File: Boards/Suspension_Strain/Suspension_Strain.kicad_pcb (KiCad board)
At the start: 2 copper layers, 57.2 x 57.2 mm, 146 parts, among them J1 CONN_02X03, J101 MM_F_RA_20, J102 MM_F_RA_08, U1 MCP2561-E_SN, U1001 MCP6001T-I-LT, U101 TPS560430YF, U102 74HC4051, U1101 MCP6001T-I-LT, U1201 MCP6001T-I-LT, U1301 MCP6001T-I-LT, U1401 MCP6001T-I-LT, U2 ATMEGA16M1, U301 MCP6001T-I-LT, U401 MCP6001T-I-LT, U501 MCP6001T-I-LT, U601 MCP6001T-I-LT, U701 MCP6001T-I-LT, U801 MCP6001T-I-LT, U901 MCP6001T-I-LT, Y1 Crystal_SMD

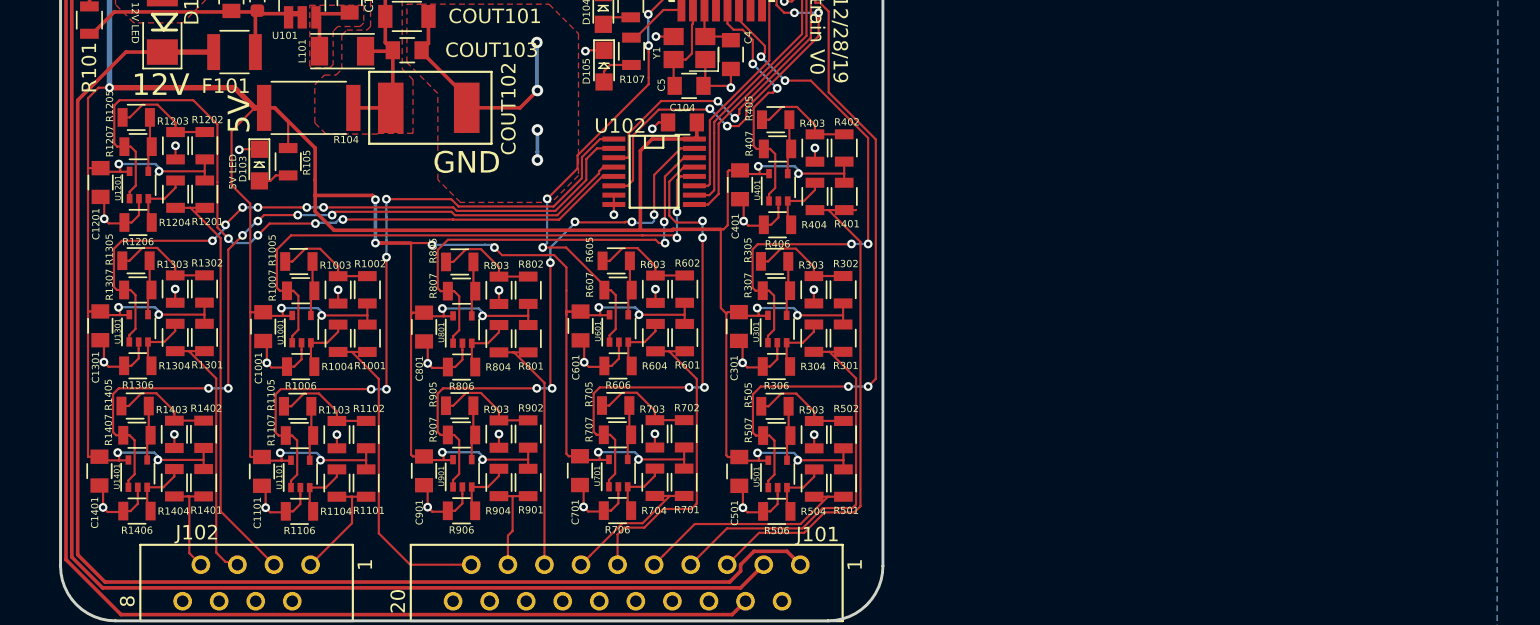
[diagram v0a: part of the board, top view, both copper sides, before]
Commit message: Remove excessive differential amplifiers
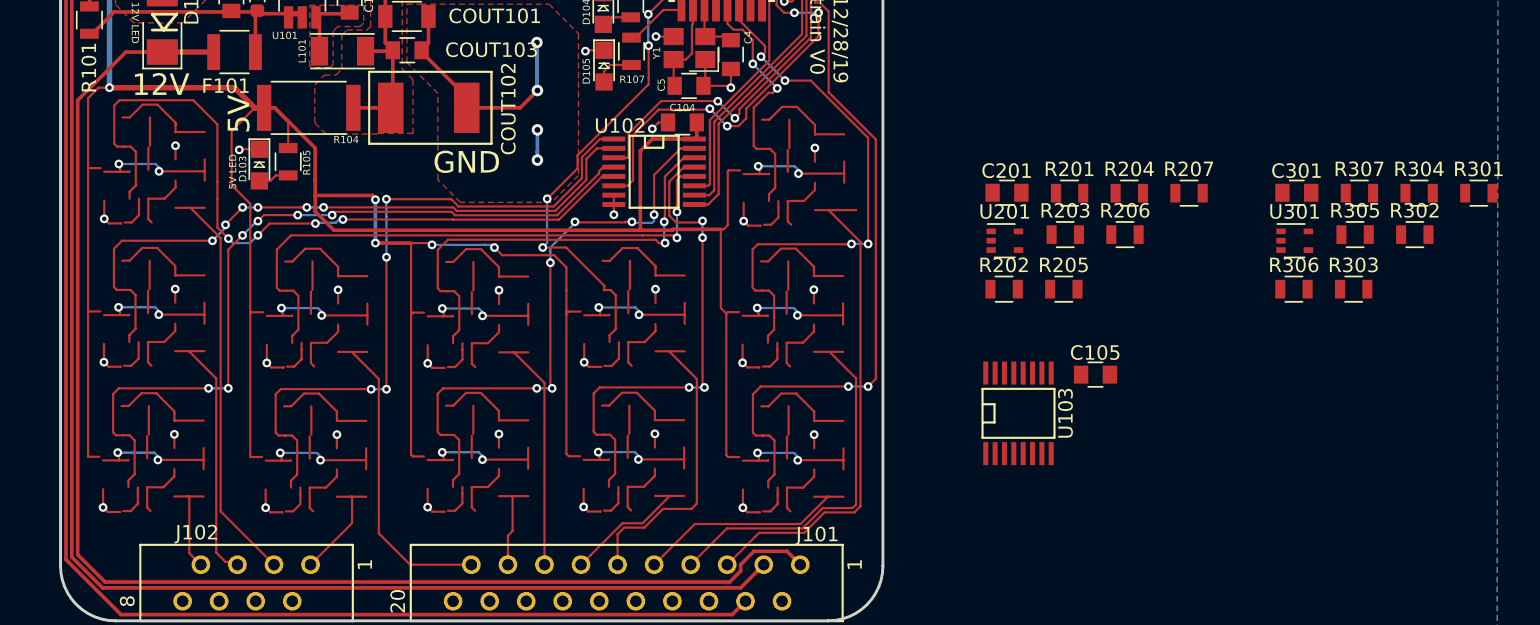
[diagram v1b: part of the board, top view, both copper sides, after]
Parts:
- removed C1001, C1101, C1201, C1301, C1401, C401, C501, C601, C701, C801, C901: C_0.1uF, footprints:C_0805_OEM
- removed G***: LOGO, footprints:Logo_Large
- removed R1001, R1002, R1003, R1004, R1005, R1101, R1102, R1103, R1104, R1105, R1201, R1202, R1203, R1204, R1205, R1301, R1302, R1303, R1304, R1305, R1401, R1402, R1403, R1404, R1405, R401, R402, R403, R404, R405, R501, R502, R503, R504, R505, R601, R602, R603, R604, R605, R701, R702, R703, R704, R705, R801, R802, R803, R804, R805, R901, R902, R903, R904, R905: R_120, footprints:R_0805_OEM
- removed R1006, R1007, R1106, R1107, R1206, R1207, R1306, R1307, R1406, R1407, R406, R407, R506, R507, R606, R607, R706, R707, R806, R807, R906, R907: R_4.99K, footprints:R_0805_OEM
- removed U1001, U1101, U1201, U1301, U1401, U401, U501, U601, U701, U801, U901: MCP6001T-I-LT, Package_TO_SOT_SMD:SOT-353_SC-70-5
- added C105: C_0.1uF, footprints:C_0805_OEM, F.Cu at (180.3, 128.1)
- added C201: C_0.1uF, footprints:C_0805_OEM, F.Cu at (174.1, 115.5)
- added R201: R_120, footprints:R_0805_OEM, F.Cu at (178.5, 115.5)
- added R202: R_120, footprints:R_0805_OEM, F.Cu at (173.9, 122.2)
- added R203: R_120, footprints:R_0805_OEM, F.Cu at (178.2, 118.4)
- added R204: R_120, footprints:R_0805_OEM, F.Cu at (182.6, 115.5)
- added R205: R_120, footprints:R_0805_OEM, F.Cu at (178.1, 122.2)
- added R206: R_4.99K, footprints:R_0805_OEM, F.Cu at (182.3, 118.4)
- added R207: R_4.99K, footprints:R_0805_OEM, F.Cu at (186.8, 115.5)
- added U103: 74HC4051, footprints:TSSOP-16-OEM, F.Cu at (174.9, 130.8)
- added U201: MCP6001T-I-LT, Package_TO_SOT_SMD:SOT-353_SC-70-5, F.Cu at (174.0, 118.8)
- moved R301 45.3 mm to (206.9, 115.5), turned to 0 degrees
- moved R304 43.3 mm to (202.8, 115.5), turned to 0 degrees
- moved R307 41.1 mm to (198.6, 115.5)
- moved R305 40.4 mm to (198.3, 118.4), turned to 0 degrees
- moved R302 39.9 mm to (202.5, 118.4), turned to 0 degrees
- moved C301 39.9 mm to (194.3, 115.5), turned to 0 degrees
- moved R303 37.5 mm to (198.2, 122.2), turned to 0 degrees
- moved U301 36.5 mm to (194.1, 118.8), turned to 0 degrees
- moved R306 36.4 mm to (194.1, 122.2), turned to 0 degrees
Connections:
- J101 pad 11: /strain_gauge_cluster/r_strain_4_+ -> Net-(J101-Pad11)
- J101 pad 13: /strain_gauge_cluster/r_strain_5_+ -> Net-(J101-Pad13)
- J101 pad 15: /strain_gauge_cluster/r_strain_6_+ -> Net-(J101-Pad15)
- J101 pad 17: /strain_gauge_cluster/r_strain_7_+ -> Net-(J101-Pad17)
- J101 pad 19: /strain_gauge_cluster/r_strain_8_+ -> Net-(J101-Pad19)
- J101 pad 5: /strain_gauge_cluster/r_strain_1_+ -> Net-(J101-Pad5)
- J101 pad 7: /strain_gauge_cluster/r_strain_2_+ -> Net-(J101-Pad7)
- J101 pad 9: /strain_gauge_cluster/r_strain_3_+ -> Net-(J101-Pad9)
- J102 pad 1: /strain_gauge_cluster/r_strain_9_+ -> Net-(J102-Pad1)
- J102 pad 3: /strain_gauge_cluster/r_strain_10_+ -> Net-(J102-Pad3)
- J102 pad 5: /strain_gauge_cluster/r_strain_11_+ -> Net-(J102-Pad5)
- J102 pad 7: /strain_gauge_cluster/r_strain_12_+ -> Net-(J102-Pad7)
- R301 pad 1: /strain_gauge_cluster/r_strain_2_+ -> /mux_2_out_to_sg
- R304 pad 2: /strain_gauge_cluster/r_strain_2_+ -> /mux_2_out_to_sg
- R307 pad 1: /sg_to_atmega_adc_3 -> /sg_to_atmega_adc_6
- U102 pad 1: /sg_to_mux_Y4 -> Net-(J101-Pad13)
- U102 pad 12: /sg_to_mux_Y3 -> Net-(J101-Pad11)
- U102 pad 13: /sg_to_mux_Y0 -> Net-(J101-Pad5)
- U102 pad 14: /sg_to_mux_Y1 -> Net-(J101-Pad7)
- U102 pad 15: /sg_to_mux_Y2 -> Net-(J101-Pad9)
- U102 pad 2: /sg_to_mux_Y6 -> Net-(J101-Pad17)
- U102 pad 3: /mux_out_to_atmega_adc_6 -> /mux_1_out_to_sg
- U102 pad 4: /sg_to_mux_Y7 -> Net-(J101-Pad19)
- U102 pad 5: /sg_to_mux_Y5 -> Net-(J101-Pad15)
- U2 pad 13: /sg_to_atmega_adc_2 -> (no net)
- U2 pad 14: /sg_to_atmega_adc_3 -> (no net)
- U2 pad 16: /sg_to_atmega_adc_5 -> (no net)
- U2 pad 26: /mux_out_to_atmega_adc_6 -> /sg_to_atmega_adc_6
- U301 pad 1: /sg_to_atmega_adc_3 -> /sg_to_atmega_adc_6
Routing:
- net (no net): track 0.00 -> 93.9 mm, vias 0 -> 12
- net Net-(J101-Pad19): track 0.00 -> 78.0 mm, vias 0 -> 6
- net Net-(J101-Pad15): track 0.00 -> 70.7 mm, vias 0 -> 4
- net Net-(J101-Pad5): track 0.00 -> 69.8 mm, vias 0 -> 4
- net Net-(J101-Pad11): track 0.00 -> 63.6 mm, vias 0 -> 2
- net Net-(J101-Pad13): track 0.00 -> 58.0 mm, vias 0 -> 4
- net Net-(J101-Pad7): track 0.00 -> 58.0 mm, vias 0 -> 2
- net Net-(J101-Pad9): track 0.00 -> 56.7 mm, vias 0 -> 6
- net /sg_to_mux_Y7: track 55.2 -> 0.00 mm, vias 6 -> 0
- net Net-(J101-Pad17): track 0.00 -> 53.6 mm, vias 0 -> 6
- net /sg_to_mux_Y5: track 53.0 -> 0.00 mm, vias 4 -> 0
- net /sg_to_mux_Y4: track 47.8 -> 0.00 mm, vias 4 -> 0
- net /sg_to_mux_Y6: track 46.7 -> 0.00 mm, vias 6 -> 0
- net /sg_to_mux_Y3: track 41.7 -> 0.00 mm, vias 2 -> 0
- net /sg_to_mux_Y2: track 40.6 -> 0.00 mm, vias 6 -> 0
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
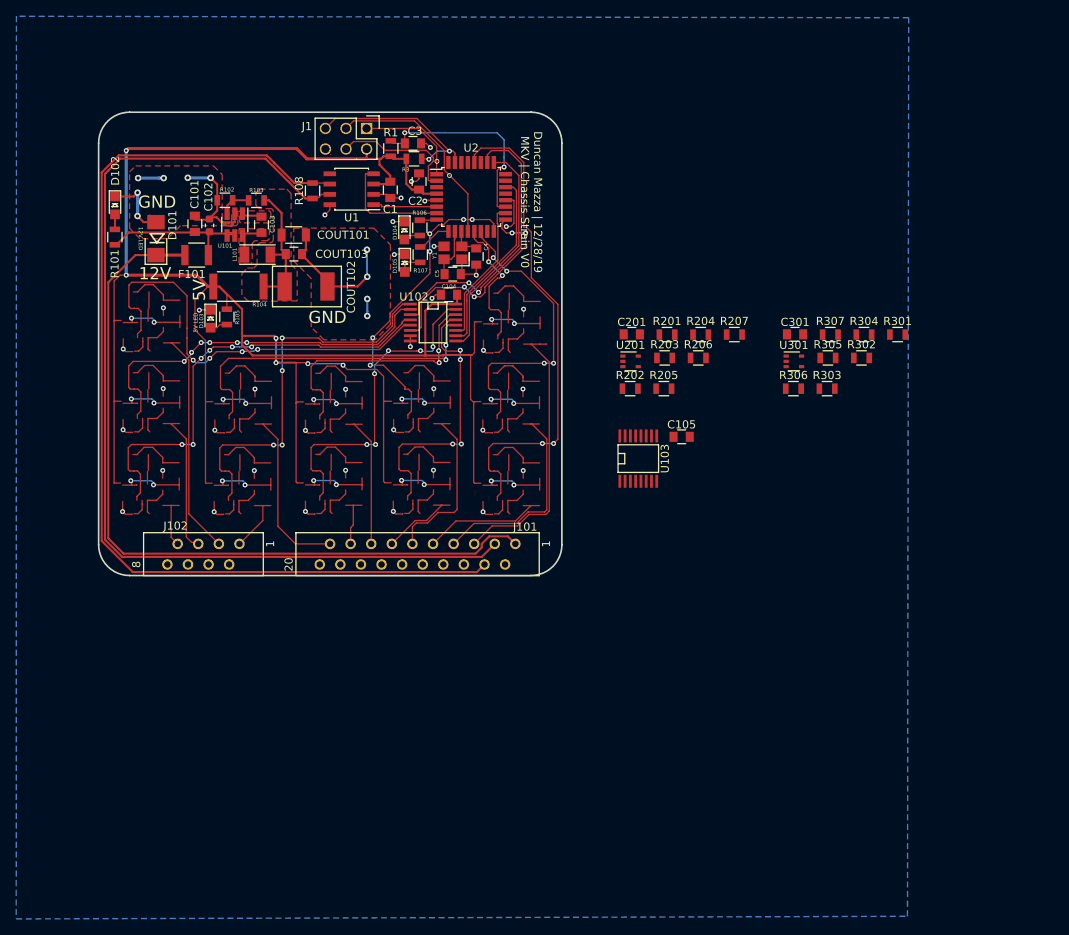
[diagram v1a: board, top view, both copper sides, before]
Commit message: Add in-progress changes for reducing noise and component use
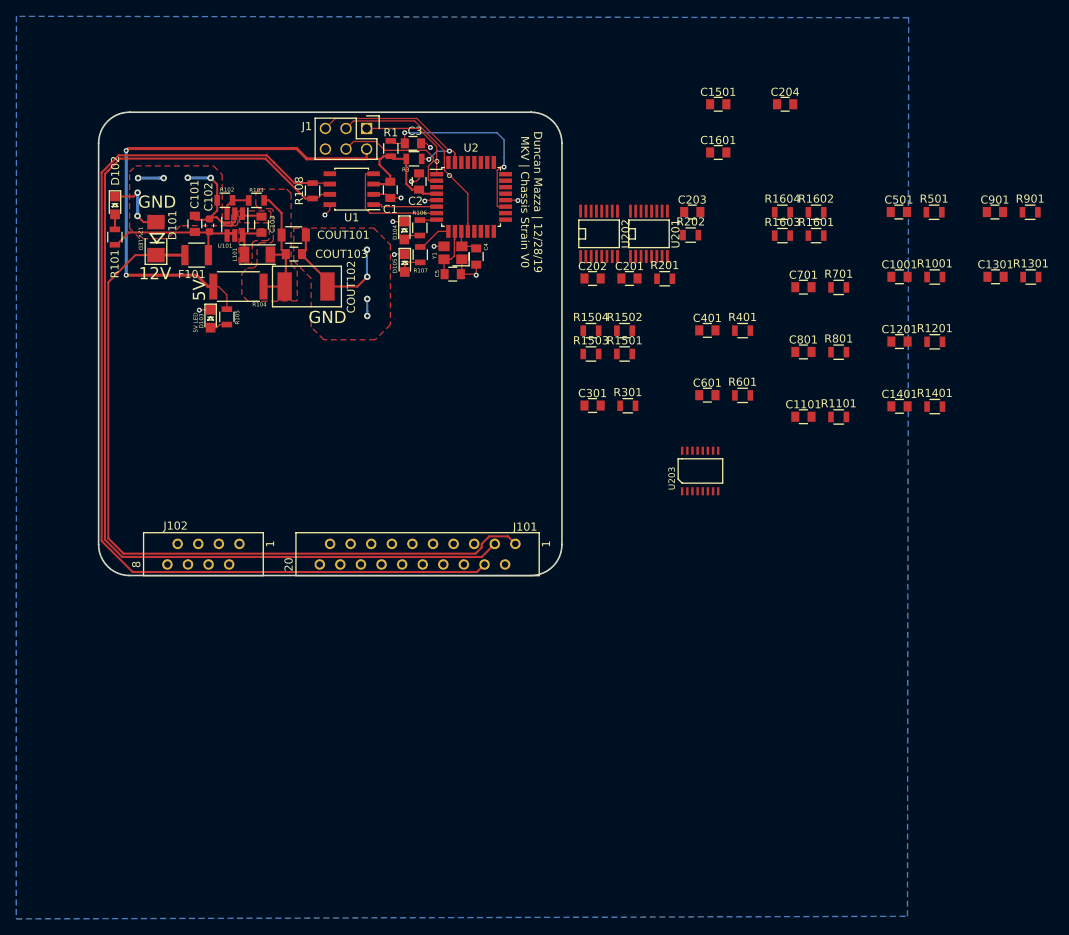
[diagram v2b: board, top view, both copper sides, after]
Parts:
- removed C104, C105: C_0.1uF, footprints:C_0805_OEM
- removed R203, R204, R205, R302, R303, R304, R305: R_120, footprints:R_0805_OEM
- removed R206, R207, R306, R307: R_4.99K, footprints:R_0805_OEM
- removed U102, U103: 74HC4051, footprints:TSSOP-16-OEM
- removed U301: MCP6001T-I-LT, Package_TO_SOT_SMD:SOT-353_SC-70-5
- added C1001: C_0.1uF, footprints:C_0805_OEM, F.Cu at (207.1, 108.4)
- added C1101: C_0.1uF, footprints:C_0805_OEM, F.Cu at (195.3, 125.7)
- added C1201: C_0.1uF, footprints:C_0805_OEM, F.Cu at (207.1, 116.4)
- added C1301: C_0.1uF, footprints:C_0805_OEM, F.Cu at (219.0, 108.4)
- added C1401: C_0.1uF, footprints:C_0805_OEM, F.Cu at (207.1, 124.4)
- added C1501: C_0.1uF, footprints:C_0805_OEM, F.Cu at (184.8, 87.1)
- added C1601: C_0.1uF, footprints:C_0805_OEM, F.Cu at (184.8, 93.1)
- added C202: C_0.1uF, footprints:C_0805_OEM, F.Cu at (169.3, 108.6)
- added C203: C_0.1uF, footprints:C_0805_OEM, F.Cu at (181.6, 100.4)
- added C204: C_0.1uF, footprints:C_0805_OEM, F.Cu at (193.0, 87.1)
- added C401: C_0.1uF, footprints:C_0805_OEM, F.Cu at (183.4, 115.0)
- added C501: C_0.1uF, footprints:C_0805_OEM, F.Cu at (207.1, 100.4)
- added C601: C_0.1uF, footprints:C_0805_OEM, F.Cu at (183.4, 123.0)
- added C701: C_0.1uF, footprints:C_0805_OEM, F.Cu at (195.3, 109.7)
- added C801: C_0.1uF, footprints:C_0805_OEM, F.Cu at (195.3, 117.7)
- added C901: C_0.1uF, footprints:C_0805_OEM, F.Cu at (218.9, 100.4)
- added R1001: R_120, footprints:R_0805_OEM, F.Cu at (211.5, 108.4)
- added R1101: R_120, footprints:R_0805_OEM, F.Cu at (199.6, 125.7)
- added R1201: R_120, footprints:R_0805_OEM, F.Cu at (211.5, 116.4)
- added R1301: R_120, footprints:R_0805_OEM, F.Cu at (223.3, 108.4)
- added R1401: R_120, footprints:R_0805_OEM, F.Cu at (211.5, 124.4)
- added R1501: R_120, footprints:R_0805_OEM, F.Cu at (173.2, 117.9)
- added R1502: R_120, footprints:R_0805_OEM, F.Cu at (173.2, 115.0)
- added R1503: R_120K, footprints:R_0805_OEM, F.Cu at (169.1, 117.9)
- added R1504: R_120K, footprints:R_0805_OEM, F.Cu at (169.1, 115.0)
- added R1601: R_120, footprints:R_0805_OEM, F.Cu at (196.9, 103.3)
- added R1602: R_120, footprints:R_0805_OEM, F.Cu at (196.9, 100.4)
- added R1603: R_120K, footprints:R_0805_OEM, F.Cu at (192.7, 103.3)
- added R1604: R_120K, footprints:R_0805_OEM, F.Cu at (192.7, 100.4)
- added R401: R_120, footprints:R_0805_OEM, F.Cu at (187.8, 115.0)
- added R501: R_120, footprints:R_0805_OEM, F.Cu at (211.4, 100.4)
- added R601: R_120, footprints:R_0805_OEM, F.Cu at (187.8, 123.0)
- added R701: R_120, footprints:R_0805_OEM, F.Cu at (199.6, 109.7)
- added R801: R_120, footprints:R_0805_OEM, F.Cu at (199.6, 117.7)
- added R901: R_120, footprints:R_0805_OEM, F.Cu at (223.3, 100.4)
- added U202: 74HC4051, footprints:TSSOP-16-OEM, F.Cu at (170.1, 103.1)
- added U203: LTC6079CGN-PBF, footprints:SSOP-16_LTC1380, F.Cu at (180.3, 129.9)
- U201: value MCP6001T-I-LT -> 74HC4051; footprint Package_TO_SOT_SMD:SOT-353_SC-70-5 -> footprints:TSSOP-16-OEM
- moved R301 34.4 mm to (173.6, 124.3)
- moved C301 26.5 mm to (169.3, 124.3)
- moved R202 20.4 mm to (181.4, 103.3)
- moved U201 15.9 mm to (176.2, 103.1)
- moved C201 6.89 mm to (173.8, 108.6)
- moved R201 6.89 mm to (178.2, 108.6)
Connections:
- J101 pad 11: Net-(J101-Pad11) -> /wsb_container/s4_+
- J101 pad 13: Net-(J101-Pad13) -> /wsb_container/s5_+
- J101 pad 15: Net-(J101-Pad15) -> /wsb_container/s6_+
- J101 pad 17: Net-(J101-Pad17) -> /wsb_container/s7_+
- J101 pad 19: Net-(J101-Pad19) -> /wsb_container/s8_+
- J101 pad 5: Net-(J101-Pad5) -> /wsb_container/s1_+
- J101 pad 7: Net-(J101-Pad7) -> /wsb_container/s2_+
- J101 pad 9: Net-(J101-Pad9) -> /wsb_container/s3_+
- J102 pad 1: Net-(J102-Pad1) -> /wsb_container/s9_+
- J102 pad 3: Net-(J102-Pad3) -> /wsb_container/s10_+
- J102 pad 5: Net-(J102-Pad5) -> /wsb_container/s11_+
- J102 pad 7: Net-(J102-Pad7) -> /wsb_container/s12_+
- R201 pad 1: /mux_1_out_to_sg -> VCC
- R201 pad 2: VCC -> /wsb_container/ref
- R202 pad 1: Net-(R202-Pad1) -> /wsb_container/ref
- R202 pad 2: VCC -> GND
- R301 pad 1: /mux_2_out_to_sg -> /wsb_container/s1_+
- U2 pad 26: /sg_to_atmega_adc_6 -> /amp_2_out
- U2 pad 28: /sg_to_atmega_adc_4 -> /amp_1_out
- U201 pad 1: /sg_to_atmega_adc_4 -> /wsb_container/s4_+
- U201 pad 2: GND -> /wsb_container/s2_+
- U201 pad 3: Net-(R204-Pad1) -> /mux_select_S0
- U201 pad 4: Net-(R205-Pad1) -> /wsb_container/s1_+
- U201 pad 5: VCC -> /wsb_container/s3_+
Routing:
- net VCC: track 383.2 -> 80.2 mm, vias 30 -> 2
- net (no net): track 93.9 -> 0.00 mm, vias 12 -> 0
- net Net-(J101-Pad19): track 78.0 -> 0.00 mm, vias 6 -> 0
- net GND: track 145.0 -> 68.3 mm, vias 47 -> 21
- net Net-(J101-Pad15): track 70.7 -> 0.00 mm, vias 4 -> 0
- net Net-(J101-Pad5): track 69.8 -> 0.00 mm, vias 4 -> 0
- net Net-(J101-Pad11): track 63.6 -> 0.00 mm, vias 2 -> 0
- net /sg_to_atmega_adc_4: track 61.1 -> 0.00 mm, vias 2 -> 0
- net Net-(J101-Pad13): track 58.0 -> 0.00 mm, vias 4 -> 0
- net Net-(J101-Pad7): track 58.0 -> 0.00 mm, vias 2 -> 0
- net Net-(J101-Pad9): track 56.7 -> 0.00 mm, vias 6 -> 0
- net Net-(J101-Pad17): track 53.6 -> 0.00 mm, vias 6 -> 0
- net /mux_out_to_atmega_adc_6: track 35.6 -> 0.00 mm, vias 2 -> 0
- net Net-(J102-Pad3): track 29.2 -> 0.00 mm
- net /mux_select_S2: track 28.0 -> 0.00 mm
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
